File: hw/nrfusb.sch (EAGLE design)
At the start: 37 parts, among them J1 MF-CON-MICROUSB-RIGHT, J3 JST-ZH6SMT_VERT, M1 MOUNT, M2 MOUNT, M3 MOUNT, M4 MOUNT, U1 MF-REG-SOT235-3.3V-300mA, U2 USBLC6-2SC6, U3 TCAN334GSOT23, U4 TLP3317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

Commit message: Nominally complete board and schematic
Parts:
- removed R5: 100, mfpassives:RESISTOR_0805
- removed R6: 330, mfpassives:RESISTOR_0402
- removed U3: TCAN334GSOT23, fdcanusb:TCAN334GSOT23
- removed U4: TLP3317, fdcanusb:TLP3317
- added C12: 0.1uF, mfpassives:CAPACITOR_NP_0402
- C4: value 0.1uF -> 10uF; device mfpassives:CAPACITOR_NP_0402 -> mfpassives:CAPACITOR_NP_1206; MPN MF-CAP-0402-0.1uF -> MF-CAP-1206-10uF
- J2: device fdcanusb:F09H -> pinhead:PINHD-2X4; MF (none) -> WURTH; MPN (none) -> 61300821121; POPULATE 0 -> 1
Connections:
- removed net CAN_N: J2.2, U3.CANL, U4.SW2
- removed net CAN_P: J2.7, R5.P$1, U3.CANH
- removed net CAN_RX: U3.RXD, U5.PB12
- removed net CAN_SHDN: U3.SHDN, U5.PB14
- removed net CAN_STB: U3.STB, U5.PB11
- removed net CAN_TERM: U4.CATHODE, U5.PB15
- removed net CAN_TX: U3.TXD, U5.PB13
- removed net LED_CAN_RX: D2.ANODE, U5.PB4
- removed net LED_CAN_TX: D1.ANODE, U5.PB3
- removed net N$7: R5.P$2, U4.SW1
- removed net N$8: R6.P$2, U4.ANODE
- new net LED_RF_RX: D2.ANODE, U5.PB15
- new net LED_RF_TX: D1.ANODE, U5.PB14
- new net NRF_CE: J2.6, U5.PA15
- new net NRF_CS: J2.5, U5.PB6
- new net NRF_IRQ: J2.1, U5.PB7
- new net NRF_MISO: J2.2, U5.PB4
- new net NRF_MOSI: J2.3, U5.PB5
- new net NRF_SCK: J2.4, U5.PB3
- net +3V3: now also C12.P$1, J2.7; no longer R6.P$1, U3.VCC
- net GND: now also C12.P$2, J2.8; no longer J2.3, J2.5, J2.6, U3.GND
- net LED_COM: now also U5.PB13; no longer U5.PB6
- net LED_PWR: now also U5.PB12; no longer U5.PB5
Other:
- note added: "NRF"
- note added: "nrfusb (c) 2019 Josh Pieper, jjp@pobox.com Licensed under the Apache 2.0 License https://www.apache.org/licenses/LICENSE-2.0"
- note removed: "CAN"
- note removed: "fdcanusb (c) 2019 Josh Pieper, jjp@pobox.com Licensed under the Apache 2.0 License https://www.apache.org/licenses/LICENSE-2.0"
- moved on the sheet: C4

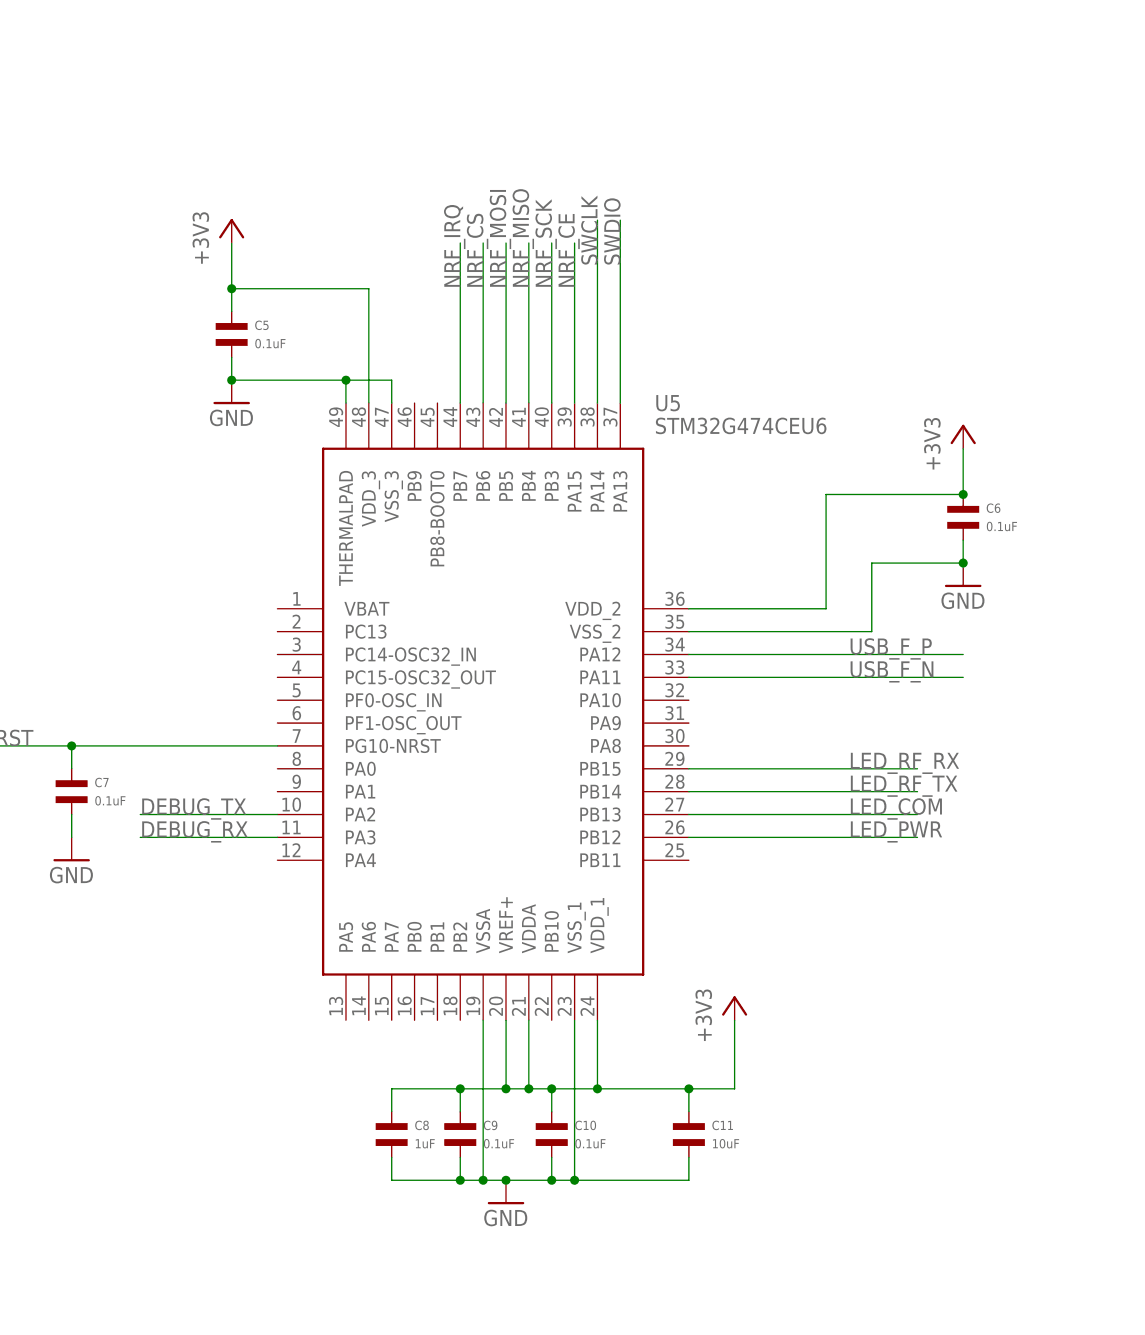
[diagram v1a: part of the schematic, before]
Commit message: Update with correct stm32 pinout
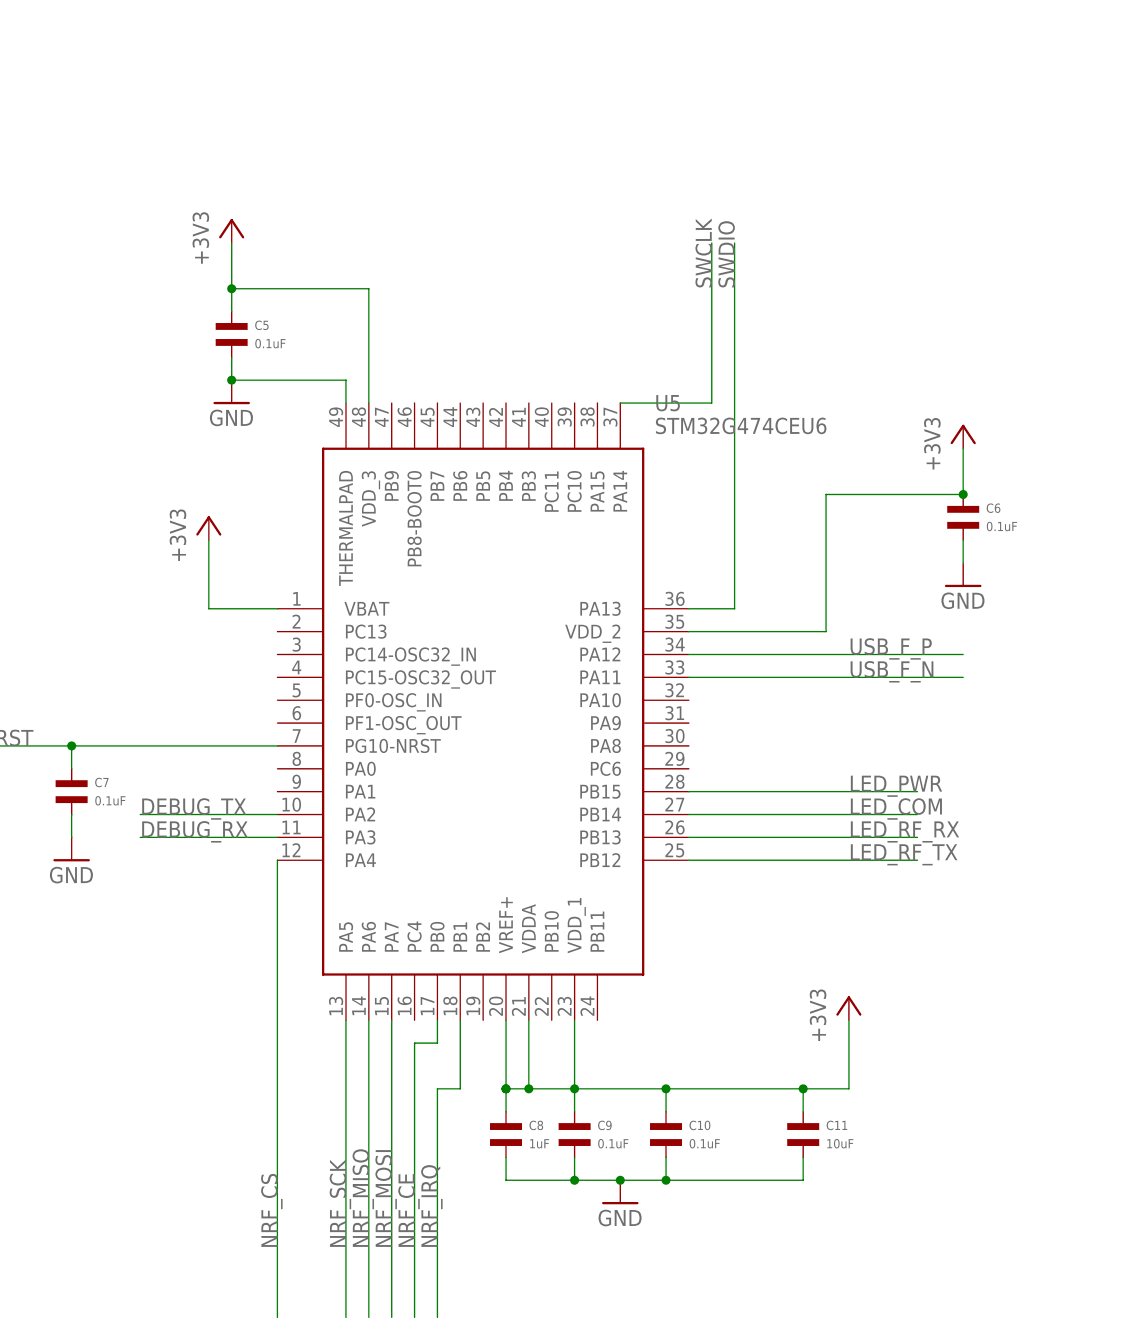
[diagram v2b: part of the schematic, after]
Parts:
- U5: device fdcanusb:STM32G474CEU6 -> nrfusb:STM32G474CEU6
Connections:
- net +3V3: now also U5.VBAT
- net GND: no longer U5.VSSA, U5.VSS_1, U5.VSS_2, U5.VSS_3
- net LED_COM: now also U5.PB14; no longer U5.PB13
- net LED_PWR: now also U5.PB15; no longer U5.PB12
- net LED_RF_RX: now also U5.PB13; no longer U5.PB15
- net LED_RF_TX: now also U5.PB12; no longer U5.PB14
- net NRF_CE: now also U5.PB0; no longer U5.PA15
- net NRF_CS: now also U5.PA4; no longer U5.PB6
- net NRF_IRQ: now also U5.PB1; no longer U5.PB7
- net NRF_MISO: now also U5.PA6; no longer U5.PB4
- net NRF_MOSI: now also U5.PA7; no longer U5.PB5
- net NRF_SCK: now also U5.PA5; no longer U5.PB3
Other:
- note added: "mjbots nrfusb r1 (c) 2020 Josh Pieper, jjp@pobox.com Licensed under the Apache 2.0 License https://www.apache.org/licenses/LICENSE-2.0"
- note removed: "nrfusb (c) 2019 Josh Pieper, jjp@pobox.com Licensed under the Apache 2.0 License https://www.apache.org/licenses/LICENSE-2.0"
- moved on the sheet: C10, C11, C8, C9
